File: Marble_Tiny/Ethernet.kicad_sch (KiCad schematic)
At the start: 41 parts, among them J3 BELFUSE_0826-1G1T-43-F, Q1 XTAL_25MHZ_EPSON_TSX-3225_25.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, U7 RTL8211F-CG

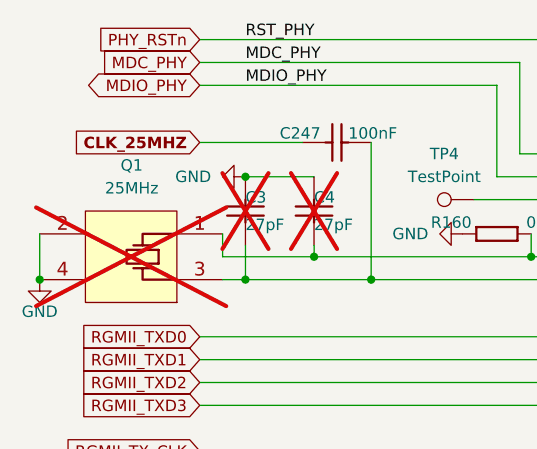
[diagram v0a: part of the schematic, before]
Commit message: connected more address lines to DDR, new board name
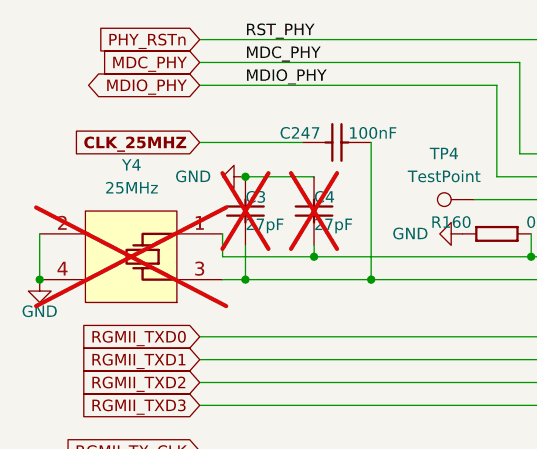
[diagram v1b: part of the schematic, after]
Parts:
- renumbered Q1 to Y4
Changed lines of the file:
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@@
 		(on_board yes)
 		(dnp yes)
-		(property "Reference" "Q1"
+		(property "Reference" "Y4"
 			(at 31.8135 58.42 0)
 			(effects
@@
 			(project ""
 				(path "/c2a4f786-b14c-434a-acf7-b20fb2221b0b/41baefe0-2999-4159-91c6-ae67dbf0b6a8"
-					(reference "Q1")
+					(reference "Y4")
 					(unit 1)
 				)
